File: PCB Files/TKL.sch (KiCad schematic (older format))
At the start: 556 parts, among them J1 USB_C, SW1 ESC, SW10 F9, SW100 RGUI_R2, SW101 RCTRL_R2, SW102 STEPPED_CAPS, SW103 RSHFT_175, SW104 Fn, SW105 BKSP_2U, SW11 F10, SW12 F11, SW13 F12, SW14 PRTSC, SW15 SCRLCK, SW16 PAUSE, SW17 GRV, SW18 1, SW19 2, SW2 F1, SW20 3, SW21 4, SW22 5, SW23 6, SW24 7, SW25 8, SW26 9, SW27 0, SW28 HIFEN, SW29 PLUS, SW3 F2, SW30 BCKSLSH, SW31 DEL, SW32 INS, SW33 HOME, SW34 PGUP, SW35 TAB, SW36 Q, SW37 W, SW38 E, SW39 R, SW4 F3, SW40 T, SW41 Y, SW42 U, SW43 I, SW44 O, SW45 P, SW46 LBRACES, SW47 RBRACES, SW48 BKSP_150, SW49 DEL, SW5 F4, SW50 END, SW51 PGDN, SW52 CAPS, SW53 A, SW54 S, SW55 D, SW56 F, SW57 G, SW58 H, SW59 J, SW6 F5, SW60 K, SW61 L, SW62 :, SW63 QUOTE, SW64 ENTER, SW65 LSHFT, SW66 Z, SW67 X, SW68 C, SW69 V, SW7 F6, SW70 B, SW71 N, SW72 M, SW73 <,, SW74 .>, SW75 /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

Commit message: Routed first 4 RGB LEDs
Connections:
- net at U102.5 (DO): now also RD52.1; no longer RD64.2
- net at RD102.2: now also U53.5 (DO); no longer U51.5 (DO)
- new net: RD64.2, U51.5 (DO)
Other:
- moved on the sheet: C102, C53, C54, C55, C56, C57, C58, C59, C60, C61, C62, C63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

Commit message: Route fourth row
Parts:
- renumbered RD53 to RD54, RD54 to RD55, RD55 to RD56, RD56 to RD57, RD57 to RD58, RD58 to RD59, RD59 to RD60, RD60 to RD61, RD61 to RD62, RD62 to RD63, RD63 to RD64, RD64 to RDR2
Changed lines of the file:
@@
 	41325 16975 41325 18025
 $Comp
-L Device:R_Small RD62
+L Device:R_Small RD63
 U 1 1 60BBF342
 P 36775 17925
-F 0 "RD62" V 36626 17925 30  0000 C CNN
+F 0 "RD63" V 36626 17925 30  0000 C CNN
 F 1 "33R" V 36686 17925 30  0000 C CNN
 F 2 "Resistor_SMD:R_0805_2012Metric" H 36775 17925 50  0001 C CNN
@@
 	38825 16975 38825 18025
 $Comp
-L Device:R_Small RD61
+L Device:R_Small RD62
 U 1 1 60BBF381
 P 34275 17925
-F 0 "RD61" V 34126 17925 30  0000 C CNN
+F 0 "RD62" V 34126 17925 30  0000 C CNN
 F 1 "33R" V 34186 17925 30  0000 C CNN
 F 2 "Resistor_SMD:R_0805_2012Metric" H 34275 17925 50  0001 C CNN
@@
 	11350 16975 11350 18025
 $Comp
-L Device:R_Small RD53
+L Device:R_Small RD54
 U 1 1 60BBF3F8
 P 14300 17925
-F 0 "RD53" V 14151 17925 30  0000 C CNN
+F 0 "RD54" V 14151 17925 30  0000 C CNN
 F 1 "33R" V 14211 17925 30  0000 C CNN
 F 2 "Resistor_SMD:R_0805_2012Metric" H 14300 17925 50  0001 C CNN
@@
 	16350 16975 16350 18025
 $Comp
-L Device:R_Small RD54
+L Device:R_Small RD55
 U 1 1 60BBF437
 P 16800 17925
-F 0 "RD54" V 16651 17925 30  0000 C CNN
+F 0 "RD55" V 16651 17925 30  0000 C CNN
 F 1 "33R" V 16711 17925 30  0000 C CNN
 F 2 "Resistor_SMD:R_0805_2012Metric" H 16800 17925 50  0001 C CNN
@@
 	18850 16975 18850 18025
 $Comp
-L Device:R_Small RD55
+L Device:R_Small RD56
 U 1 1 60BBF476
 P 19275 17925
-F 0 "RD55" V 19126 17925 30  0000 C CNN
+F 0 "RD56" V 19126 17925 30  0000 C CNN
 F 1 "33R" V 19186 17925 30  0000 C CNN
 F 2 "Resistor_SMD:R_0805_2012Metric" H 19275 17925 50  0001 C CNN
@@
 	21350 16975 21350 18025
 $Comp
-L Device:R_Small RD56
+L Device:R_Small RD57
 U 1 1 60BBF4B4
 P 21775 17925
-F 0 "RD56" V 21626 17925 30  0000 C CNN
+F 0 "RD57" V 21626 17925 30  0000 C CNN
 F 1 "33R" V 21686 17925 30  0000 C CNN
 F 2 "Resistor_SMD:R_0805_2012Metric" H 21775 17925 50  0001 C CNN
@@
 	21350 18025 21950 18025
 $Comp
-L Device:R_Small RD57
+L Device:R_Small RD58
 U 1 1 60BBF4F4
 P 24275 17925
-F 0 "RD57" V 24126 17925 30  0000 C CNN
+F 0 "RD58" V 24126 17925 30  0000 C CNN
 F 1 "33R" V 24186 17925 30  0000 C CNN
 F 2 "Resistor_SMD:R_0805_2012Metric" H 24275 17925 50  0001 C CNN
@@
 	29825 18375 29825 18325
 $Comp
-L Device:R_Small RD59
+L Device:R_Small RD60
 U 1 1 60BBF56B
 P 29250 17925
-F 0 "RD59" V 29101 17925 30  0000 C CNN
+F 0 "RD60" V 29101 17925 30  0000 C CNN
 F 1 "33R" V 29161 17925 30  0000 C CNN
 F 2 "Resistor_SMD:R_0805_2012Metric" H 29250 17925 50  0001 C CNN
@@
 	32725 18125 32750 18125
 $Comp
-L Device:R_Small RD60
+L Device:R_Small RD61
 U 1 1 60BBF57F
 P 31775 17925
-F 0 "RD60" V 31626 17925 30  0000 C CNN
+F 0 "RD61" V 31626 17925 30  0000 C CNN
 F 1 "33R" V 31686 17925 30  0000 C CNN
 F 2 "Resistor_SMD:R_0805_2012Metric" H 31775 17925 50  0001 C CNN
@@
 	33825 18025 34425 18025
 $Comp
-L Device:R_Small RD58
+L Device:R_Small RD59
 U 1 1 60BBF5B1
 P 26750 17925
-F 0 "RD58" V 26601 17925 30  0000 C CNN
+F 0 "RD59" V 26601 17925 30  0000 C CNN
 F 1 "33R" V 26661 17925 30  0000 C CNN
 F 2 "Resistor_SMD:R_0805_2012Metric" H 26750 17925 50  0001 C CNN
@@
 	9075 16975 11350 16975
 $Comp
-L Device:R_Small RD64
+L Device:R_Small RDR2
 U 1 1 60BBF616
 P 41750 17925
-F 0 "RD64" V 41601 17925 30  0000 C CNN
+F 0 "RDR2" V 41601 17925 30  0000 C CNN
 F 1 "33R" V 41661 17925 30  0000 C CNN
 F 2 "Resistor_SMD:R_0805_2012Metric" H 41750 17925 50  0001 C CNN
@@
 $EndComp
 $Comp
-L Device:R_Small RD63
+L Device:R_Small RD64
 U 1 1 60BBF61C
 P 39250 17925
-F 0 "RD63" V 39101 17925 30  0000 C CNN
+F 0 "RD64" V 39101 17925 30  0000 C CNN
 F 1 "33R" V 39161 17925 30  0000 C CNN
 F 2 "Resistor_SMD:R_0805_2012Metric" H 39250 17925 50  0001 C CNN

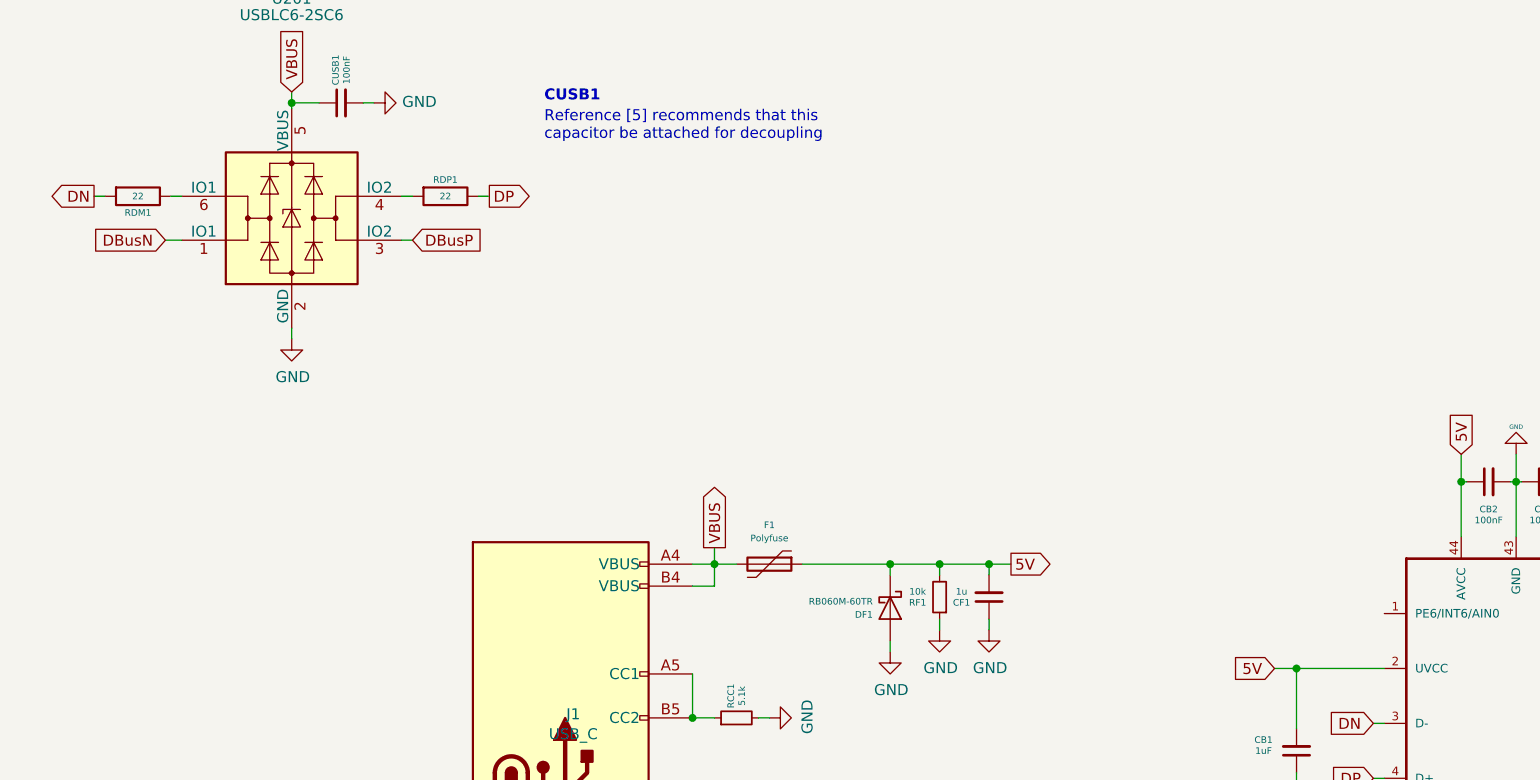
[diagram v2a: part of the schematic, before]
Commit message: Rotuted USB Connector and D+ D-
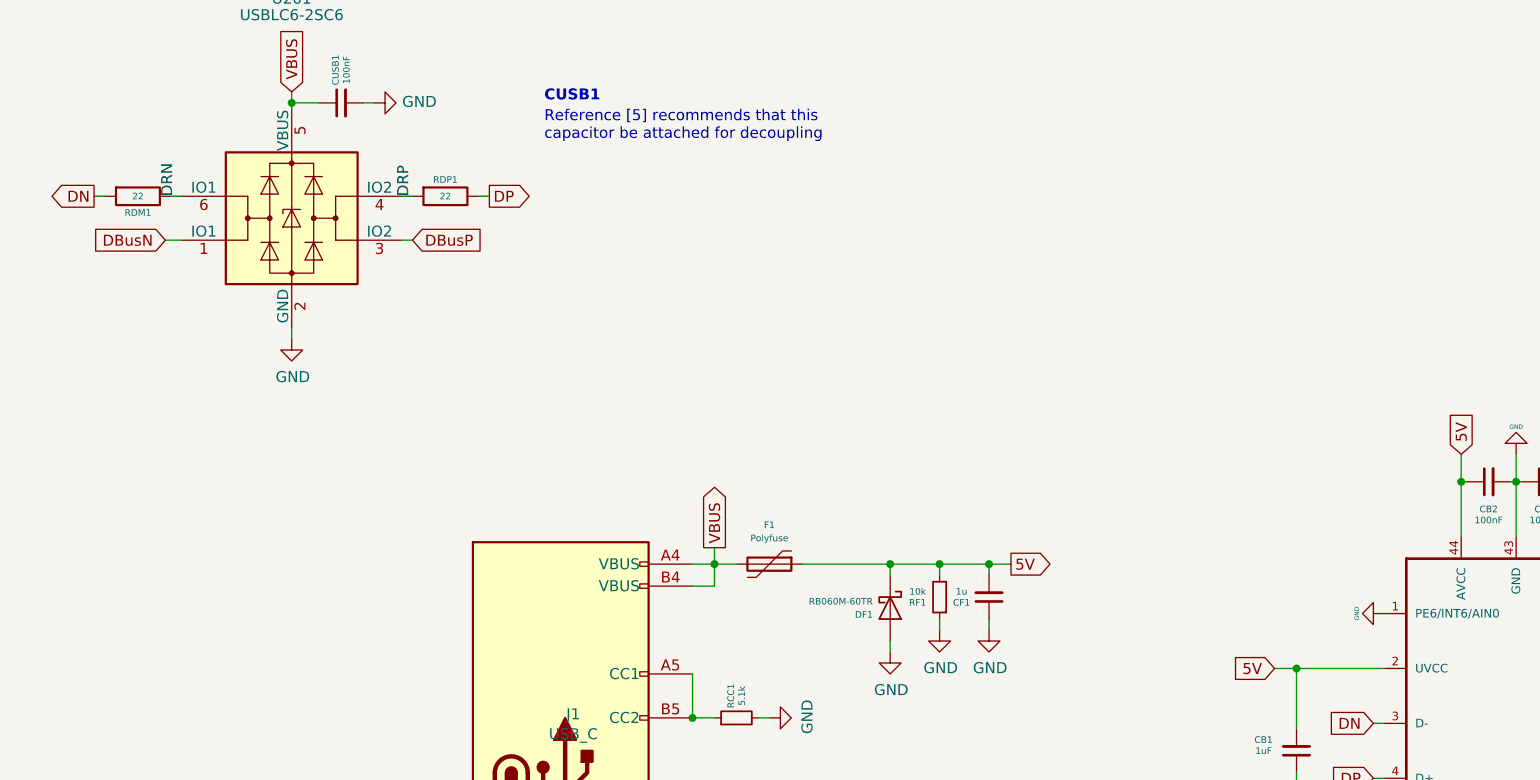
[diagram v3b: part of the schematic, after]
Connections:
- net GND: now also U200.1 (PE6/INT6/AIN0)
- net DRN: now reaches RDM1.1, U201.6 (IO1)
- net DRP: now reaches RDP1.2, U201.4 (IO2)
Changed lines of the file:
@@
 Wire Wire Line
 	13850 18025 14450 18025
+$Comp
+L power:GND #PWR0164
+U 1 1 5E9F27CA
+P 21750 -5825
+F 0 "#PWR0164" H 21750 -6075 50  0001 C CNN
+F 1 "GND" H 21750 -5950 20  0000 C CNN
+F 2 "" H 21750 -5825 50  0001 C CNN
+F 3 "" H 21750 -5825 50  0001 C CNN
+	1    21750 -5825
+	0    1    1    0
+$EndComp
+Text Label 16250 -7725 1    50   ~ 0
+DRN
+Text Label 17325 -7725 1    50   ~ 0
+DRP
 $EndSCHEMATC

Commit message: - Add license and readme, update PCB backup files
- LICENSE and README were added

- Backup for schematic and footprint library were also modified
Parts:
- RHWB1: footprint acheron_Components:R_SMD_1026 -> Resistor_SMD:R_0805_2012Metric
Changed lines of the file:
@@
 F 0 "RHWB1" V 25000 -5825 30  0000 C CNN
 F 1 "1k" V 25050 -5825 30  0000 C CNN
-F 2 "acheron_Components:R_SMD_1026" V 25080 -5825 50  0001 C CNN
+F 2 "Resistor_SMD:R_0805_2012Metric" V 25080 -5825 50  0001 C CNN
 F 3 "~" H 25150 -5825 50  0001 C CNN
 	1    25150 -5825

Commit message: Rename RGB 3rd row RD annotation
- Fixed a small isue where resistors RD in the 3RD row of RGB controllers were misannotated: they were all a number ahead (i.e., where it should be RD(X) was RD(X+1))
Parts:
- renumbered RD54 to RD53, RD55 to RD54, RD56 to RD55, RD57 to RD56, RD58 to RD57, RD59 to RD58, RD60 to RD59, RD61 to RD60, RD62 to RD61, RD63 to RD62, RD64 to RD63, RDR2 to RD64
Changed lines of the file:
@@
 	41325 16975 41325 18025
 $Comp
-L Device:R_Small RD63
+L Device:R_Small RD62
 U 1 1 60BBF342
 P 36775 17925
-F 0 "RD63" V 36626 17925 30  0000 C CNN
+F 0 "RD62" V 36626 17925 30  0000 C CNN
 F 1 "33R" V 36686 17925 30  0000 C CNN
 F 2 "Resistor_SMD:R_0805_2012Metric" H 36775 17925 50  0001 C CNN
@@
 	38825 16975 38825 18025
 $Comp
-L Device:R_Small RD62
+L Device:R_Small RD61
 U 1 1 60BBF381
 P 34275 17925
-F 0 "RD62" V 34126 17925 30  0000 C CNN
+F 0 "RD61" V 34126 17925 30  0000 C CNN
 F 1 "33R" V 34186 17925 30  0000 C CNN
 F 2 "Resistor_SMD:R_0805_2012Metric" H 34275 17925 50  0001 C CNN
@@
 	11350 16975 11350 18025
 $Comp
-L Device:R_Small RD54
+L Device:R_Small RD53
 U 1 1 60BBF3F8
 P 14300 17925
-F 0 "RD54" V 14151 17925 30  0000 C CNN
+F 0 "RD53" V 14151 17925 30  0000 C CNN
 F 1 "33R" V 14211 17925 30  0000 C CNN
 F 2 "Resistor_SMD:R_0805_2012Metric" H 14300 17925 50  0001 C CNN
@@
 	16350 16975 16350 18025
 $Comp
-L Device:R_Small RD55
+L Device:R_Small RD54
 U 1 1 60BBF437
 P 16800 17925
-F 0 "RD55" V 16651 17925 30  0000 C CNN
+F 0 "RD54" V 16651 17925 30  0000 C CNN
 F 1 "33R" V 16711 17925 30  0000 C CNN
 F 2 "Resistor_SMD:R_0805_2012Metric" H 16800 17925 50  0001 C CNN
@@
 	18850 16975 18850 18025
 $Comp
-L Device:R_Small RD56
+L Device:R_Small RD55
 U 1 1 60BBF476
 P 19275 17925
-F 0 "RD56" V 19126 17925 30  0000 C CNN
+F 0 "RD55" V 19126 17925 30  0000 C CNN
 F 1 "33R" V 19186 17925 30  0000 C CNN
 F 2 "Resistor_SMD:R_0805_2012Metric" H 19275 17925 50  0001 C CNN
@@
 	21350 16975 21350 18025
 $Comp
-L Device:R_Small RD57
+L Device:R_Small RD56
 U 1 1 60BBF4B4
 P 21775 17925
-F 0 "RD57" V 21626 17925 30  0000 C CNN
+F 0 "RD56" V 21626 17925 30  0000 C CNN
 F 1 "33R" V 21686 17925 30  0000 C CNN
 F 2 "Resistor_SMD:R_0805_2012Metric" H 21775 17925 50  0001 C CNN
@@
 	21350 18025 21950 18025
 $Comp
-L Device:R_Small RD58
+L Device:R_Small RD57
 U 1 1 60BBF4F4
 P 24275 17925
-F 0 "RD58" V 24126 17925 30  0000 C CNN
+F 0 "RD57" V 24126 17925 30  0000 C CNN
 F 1 "33R" V 24186 17925 30  0000 C CNN
 F 2 "Resistor_SMD:R_0805_2012Metric" H 24275 17925 50  0001 C CNN
@@
 	29825 18375 29825 18325
 $Comp
-L Device:R_Small RD60
+L Device:R_Small RD59
 U 1 1 60BBF56B
 P 29250 17925
-F 0 "RD60" V 29101 17925 30  0000 C CNN
+F 0 "RD59" V 29101 17925 30  0000 C CNN
 F 1 "33R" V 29161 17925 30  0000 C CNN
 F 2 "Resistor_SMD:R_0805_2012Metric" H 29250 17925 50  0001 C CNN
@@
 	32725 18125 32750 18125
 $Comp
-L Device:R_Small RD61
+L Device:R_Small RD60
 U 1 1 60BBF57F
 P 31775 17925
-F 0 "RD61" V 31626 17925 30  0000 C CNN
+F 0 "RD60" V 31626 17925 30  0000 C CNN
 F 1 "33R" V 31686 17925 30  0000 C CNN
 F 2 "Resistor_SMD:R_0805_2012Metric" H 31775 17925 50  0001 C CNN
@@
 	33825 18025 34425 18025
 $Comp
-L Device:R_Small RD59
+L Device:R_Small RD58
 U 1 1 60BBF5B1
 P 26750 17925
-F 0 "RD59" V 26601 17925 30  0000 C CNN
+F 0 "RD58" V 26601 17925 30  0000 C CNN
 F 1 "33R" V 26661 17925 30  0000 C CNN
 F 2 "Resistor_SMD:R_0805_2012Metric" H 26750 17925 50  0001 C CNN
@@
 	9075 16975 11350 16975
 $Comp
-L Device:R_Small RDR2
+L Device:R_Small RD64
 U 1 1 60BBF616
 P 41750 17925
-F 0 "RDR2" V 41601 17925 30  0000 C CNN
+F 0 "RD64" V 41601 17925 30  0000 C CNN
 F 1 "33R" V 41661 17925 30  0000 C CNN
 F 2 "Resistor_SMD:R_0805_2012Metric" H 41750 17925 50  0001 C CNN
@@
 $EndComp
 $Comp
-L Device:R_Small RD64
+L Device:R_Small RD63
 U 1 1 60BBF61C
 P 39250 17925
-F 0 "RD64" V 39101 17925 30  0000 C CNN
+F 0 "RD63" V 39101 17925 30  0000 C CNN
 F 1 "33R" V 39161 17925 30  0000 C CNN
 F 2 "Resistor_SMD:R_0805_2012Metric" H 39250 17925 50  0001 C CNN

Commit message: Add 4th RGB row
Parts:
- added C? (x16): 100nF, Capacitor_SMD:C_0805_2012Metric, symbol Device:C_Small
- added L? (x16): LED_BGRA, acheron_Components:LED_RGB_SMD_6028_2.8x3.5mm_Round, symbol Device:LED_BGRA
- added R? (x16): 100R, Resistor_SMD:R_0805_2012Metric, symbol Device:R_Small
- added RD17, RD53, RD? (x16): 33R, Resistor_SMD:R_0805_2012Metric, symbol Device:R_Small
- added U103, U104, U77, U? (x13): WS2811M, acheron_Components:MSOP-8-1EP_3x3mm_P0.65mm_EP1.68x1.88mm, symbol acheronSymbols:WS2811M
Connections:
- net 5V: now also L?.4 (A), L?.4 (A), L?.4 (A), L?.4 (A), L?.4 (A), L?.4 (A), L?.4 (A), L?.4 (A), L?.4 (A), L?.4 (A), L?.4 (A), L?.4 (A), L?.4 (A), L?.4 (A), L?.4 (A), L?.4 (A), R?.1, R?.1, R?.1, R?.1, R?.1, R?.1, R?.1, R?.1, R?.1, R?.1, R?.1, R?.1, R?.1, R?.1, R?.1, R?.1
- net GND: now also C?.2, C?.2, C?.2, C?.2, C?.2, C?.2, C?.2, C?.2, C?.2, C?.2, C?.2, C?.2, C?.2, C?.2, C?.2, C?.2, U103.4 (GND), U103.9 (GND), U104.4 (GND), U104.9 (GND), U77.4 (GND), U77.9 (GND), U?.4 (GND), U?.4 (GND), U?.4 (GND), U?.4 (GND), U?.4 (GND), U?.4 (GND), U?.4 (GND), U?.4 (GND), U?.4 (GND), U?.4 (GND), U?.4 (GND), U?.4 (GND), U?.4 (GND), U?.9 (GND), U?.9 (GND), U?.9 (GND), U?.9 (GND), U?.9 (GND), U?.9 (GND), U?.9 (GND), U?.9 (GND), U?.9 (GND), U?.9 (GND), U?.9 (GND), U?.9 (GND), U?.9 (GND)
- net RGB_DIN: now also RD?.2
- new net: L?.3 (RK), U?.1 (OUTR) (x13)
- new net: L?.2 (GK), U?.2 (OUTG) (x13)
- new net: L?.1 (BK), U?.3 (OUTB) (x13)
- new net: RD?.2, U?.5 (DO) (x13)
- new net: RD?.1, U?.6 (DIN) (x13)
- new net: C?.1, R?.2, U?.8 (VDD) (x13)
- new net: RD?.1, U103.6 (DIN)
- new net: L?.3 (RK), U103.1 (OUTR)
- new net: L?.2 (GK), U103.2 (OUTG)
- new net: L?.1 (BK), U103.3 (OUTB)
- new net: RD?.2, U103.5 (DO)
- new net: C?.1, R?.2, U103.8 (VDD)
- new net: RD?.1, U104.6 (DIN)
- new net: L?.3 (RK), U104.1 (OUTR)
- new net: L?.2 (GK), U104.2 (OUTG)
- new net: L?.1 (BK), U104.3 (OUTB)
- new net: RD?.2, U104.5 (DO)
- new net: C?.1, R?.2, U104.8 (VDD)
- new net: RD?.1, U77.6 (DIN)
- new net: L?.3 (RK), U77.1 (OUTR)
- new net: L?.2 (GK), U77.2 (OUTG)
- new net: L?.1 (BK), U77.3 (OUTB)
- new net: C?.1, R?.2, U77.8 (VDD)

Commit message: Anntate 4th RGB LED component row
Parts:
- removed RD53: 33R, Resistor_SMD:R_0805_2012Metric, symbol Device:R_Small
- gave numbers to parts that had none: 73
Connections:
- net RGB_DIN: no longer RD65.2
- net at U52.5 (DO): now also RD65.2
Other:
- moved on the sheet: C103, C104, C65, C66, C67, C68, C69, C70, C71, C72, C73, C74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

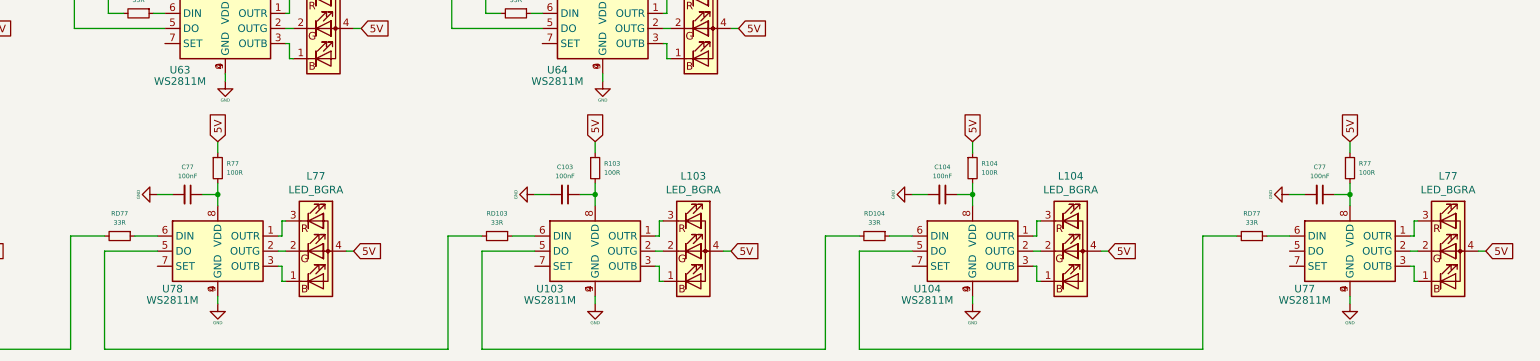
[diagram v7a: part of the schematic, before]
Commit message: Remove RGB LED 77 second instance
- There were two instances of RGB LED 77
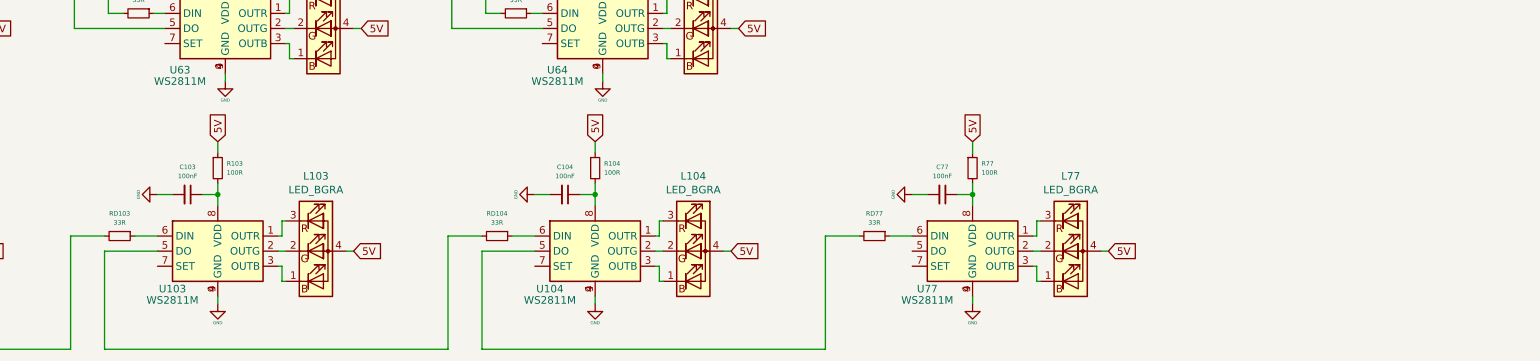
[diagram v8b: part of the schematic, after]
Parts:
- removed C77: 100nF, Capacitor_SMD:C_0805_2012Metric, symbol Device:C_Small
- removed L77: LED_BGRA, acheron_Components:LED_RGB_SMD_6028_2.8x3.5mm_Round, symbol Device:LED_BGRA
- removed R77: 100R, Resistor_SMD:R_0805_2012Metric, symbol Device:R_Small
- removed RD77: 33R, Resistor_SMD:R_0805_2012Metric, symbol Device:R_Small
- removed U78: WS2811M, acheron_Components:MSOP-8-1EP_3x3mm_P0.65mm_EP1.68x1.88mm, symbol acheronSymbols:WS2811M
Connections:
- net at U76.5 (DO): now also RD103.2
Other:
- moved on the sheet: C103, C104, C77, L103, L104, L77, R103, R104, R77, RD103, RD104, RD77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
